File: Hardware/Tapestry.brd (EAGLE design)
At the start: 100 x 80 mm, 81 parts, among them U1 ATSAMS70NXXA-AN, U2 AK4618VQ, U3 V_REG_MIC2920, U4 V_REG_MIC2920, U5 USD-SOCKETNEW, Y1 12MHZ

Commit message: Second update from Jamie
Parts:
- R15: value 330 -> 15K
- R16: value 330 -> 22K
- moved R7 65.6 mm to (8.89, 31.8)
- moved D1 64.8 mm to (8.89, 27.9), turned to 270 degrees
- moved JP2 41.2 mm to (31.8, 8.89), turned to 270 degrees
- moved C13 35.3 mm to (49.5, 47.0), turned to 90 degrees
- moved C14 31.8 mm to (52.1, 47.0), turned to 90 degrees
- moved TP2 31.0 mm to (27.9, 57.1)
- moved C15 28.2 mm to (54.6, 47.0), turned to 90 degrees
- moved U3 27.9 mm to (68.6, 15.2)
- moved U4 26.1 mm to (69.8, 34.3)
- moved C1 25.9 mm to (40.6, 43.2)
- moved C16 24.7 mm to (57.1, 47.0), turned to 90 degrees
- moved C38 22.6 mm to (66.0, 57.1)
- moved C37 22.6 mm to (66.0, 53.3)
- moved TP3 21.8 mm to (6.35, 55.9)
- moved C17 21.1 mm to (59.7, 47.0), turned to 90 degrees
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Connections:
- removed net RD: TP2.6
- removed net TD: TP2.5
- net TDMI: now also TP2.6
- net TDMO: now also TP2.5
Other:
- board size 100 x 80 mm -> 96.2 x 67.3 mm

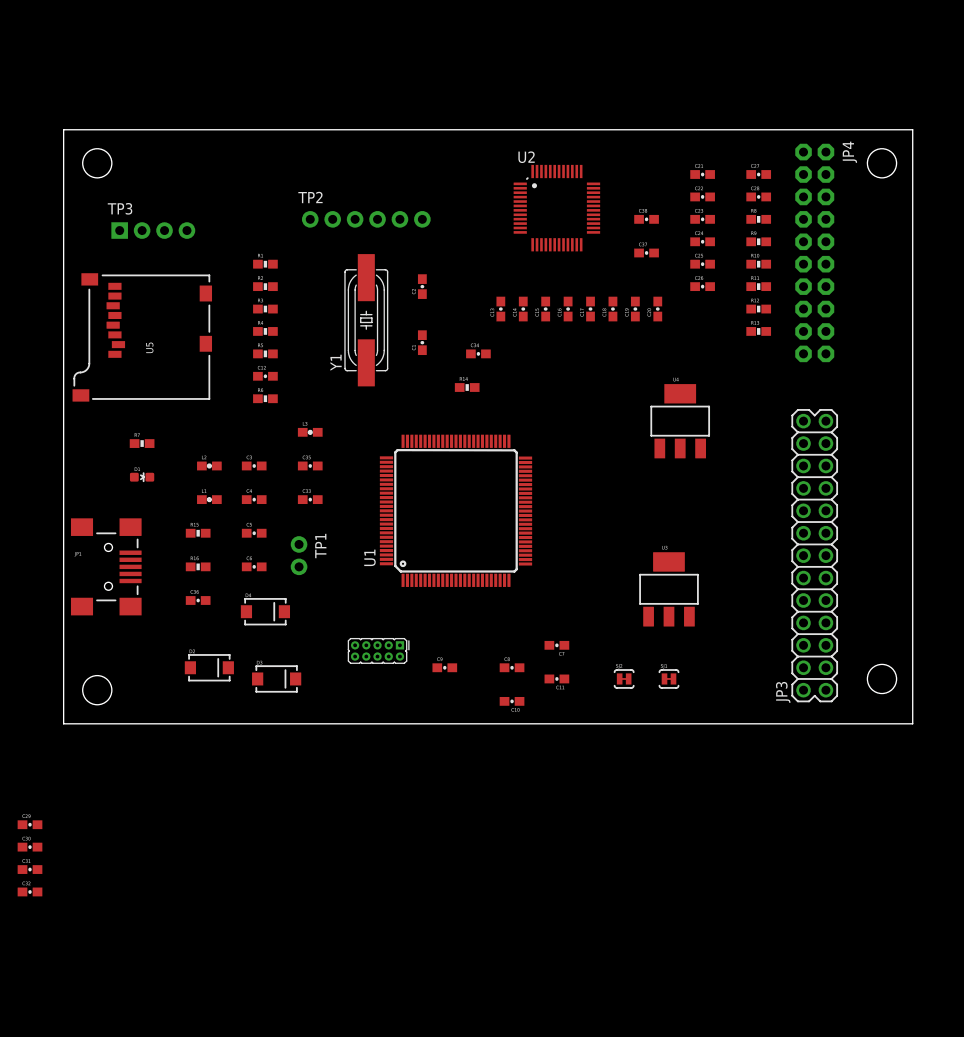
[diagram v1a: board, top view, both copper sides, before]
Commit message: Fixed unconnected nets and missing cap values.
Signed-off-by: robertsonics <jamie@robertsonics.com>
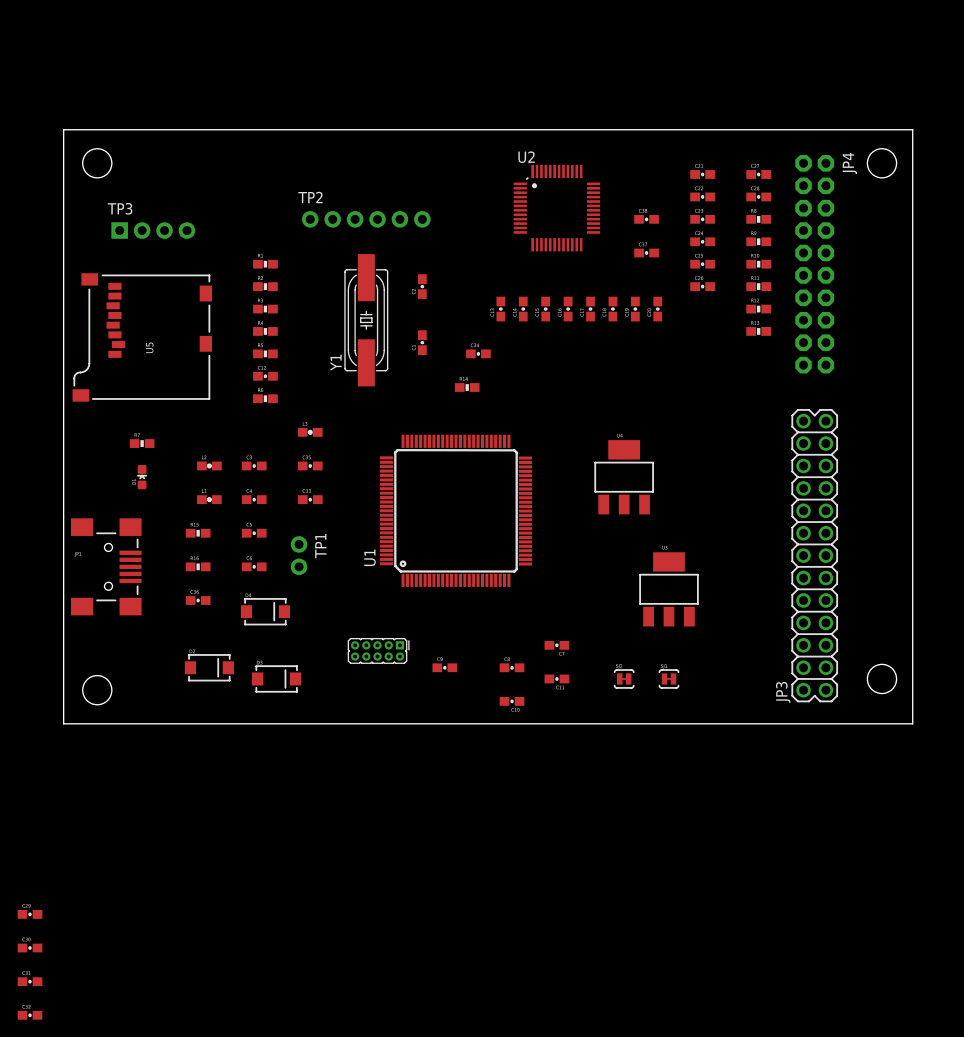
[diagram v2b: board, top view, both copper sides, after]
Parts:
- C29, C30, C31, C32: value (none) -> 0.1uF
- D1: value (none) -> BLUE
- moved C32 14.0 mm to (-3.81, -33.0)
- moved C31 12.7 mm to (-3.81, -29.2)
- moved C30 11.4 mm to (-3.81, -25.4)
- moved C29 10.2 mm to (-3.81, -21.6)
- moved U4 8.98 mm to (63.5, 27.9)
- moved JP4 1.27 mm to (85.1, 52.1)
- turned D1 to 0 degrees
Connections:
- removed net JP1: JP2.1
- removed net N$24: SJ2.2
- removed net TCK: JP2.4
- removed net TMS: JP2.2
- net 3.3V: now also JP2.1
- net 3.3V_A: now also SJ2.2
- net SWCLK/TCK: now also JP2.4
- net SWDIO/TMS: now also JP2.2

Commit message: Replaced generic resistors and capacitors with SparkFun versions.
Signed-off-by: robertsonics <jamie@robertsonics.com>
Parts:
- C13, C15, C17, C19, C20, C21, C22, C23, C24, C25, C26, C27, C28, C37, C38: value 1uF -> 1.0uF
- C34: value 10p -> 10pF
- R1, R8: value 100K -> 100k
- R5: value 10k -> 10K

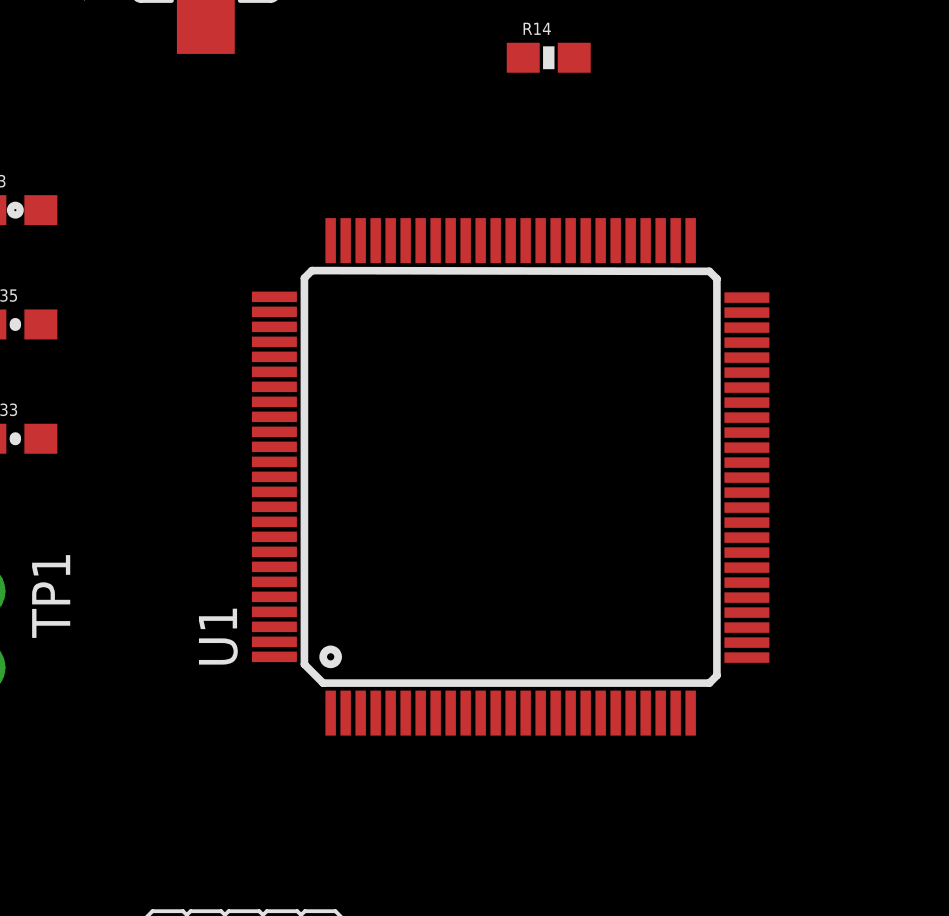
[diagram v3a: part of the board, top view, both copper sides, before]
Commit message: First pass over schematic.
Mostly changing flag style on signals.
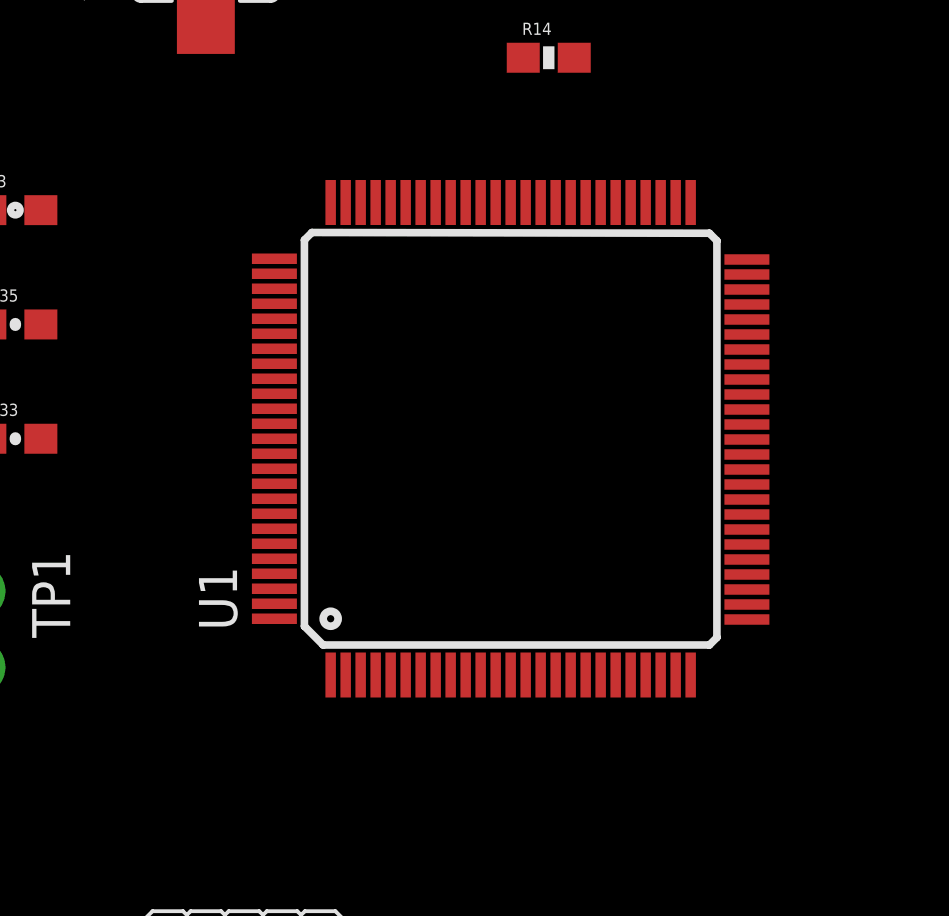
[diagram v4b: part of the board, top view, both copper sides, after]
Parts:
- moved U1 1.27 mm to (44.5, 25.4)

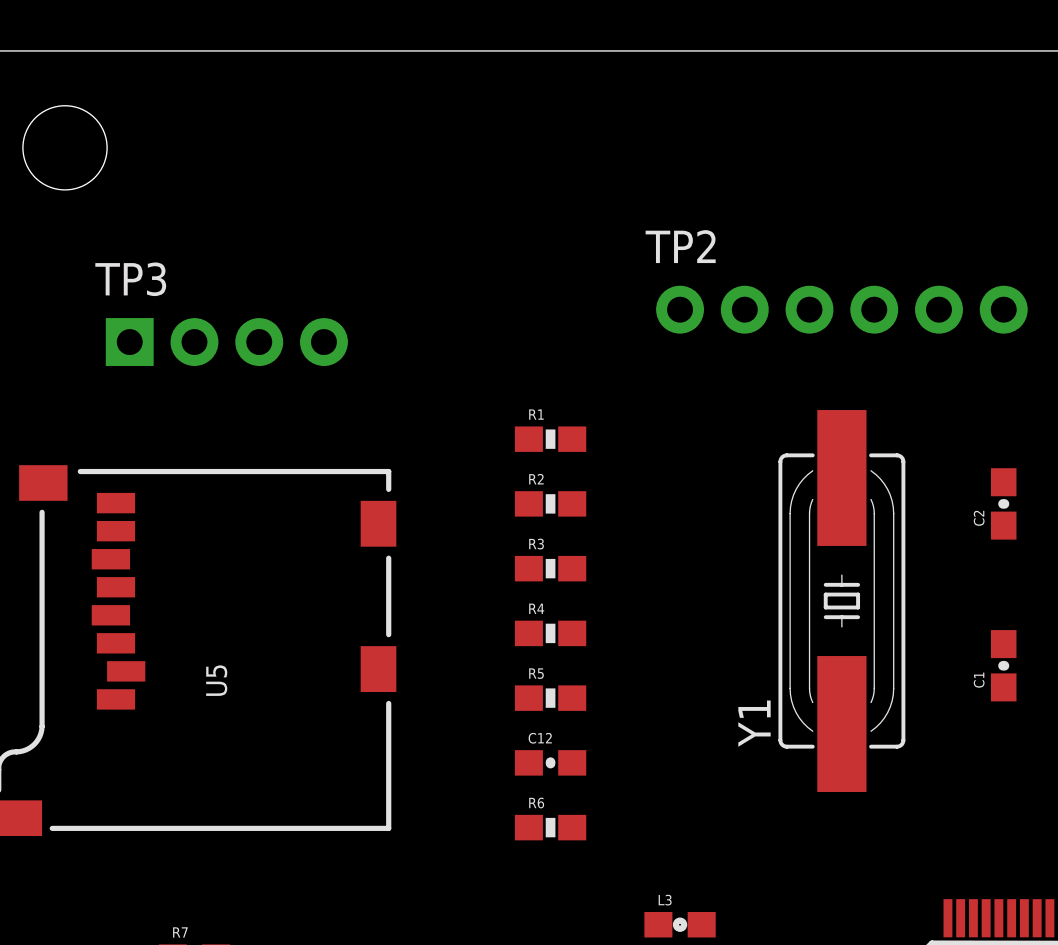
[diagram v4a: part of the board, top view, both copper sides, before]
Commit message: Second pass over schematic
-Swapped crystal for smaller one.
-Updated SD card connector with SDIO signal names.
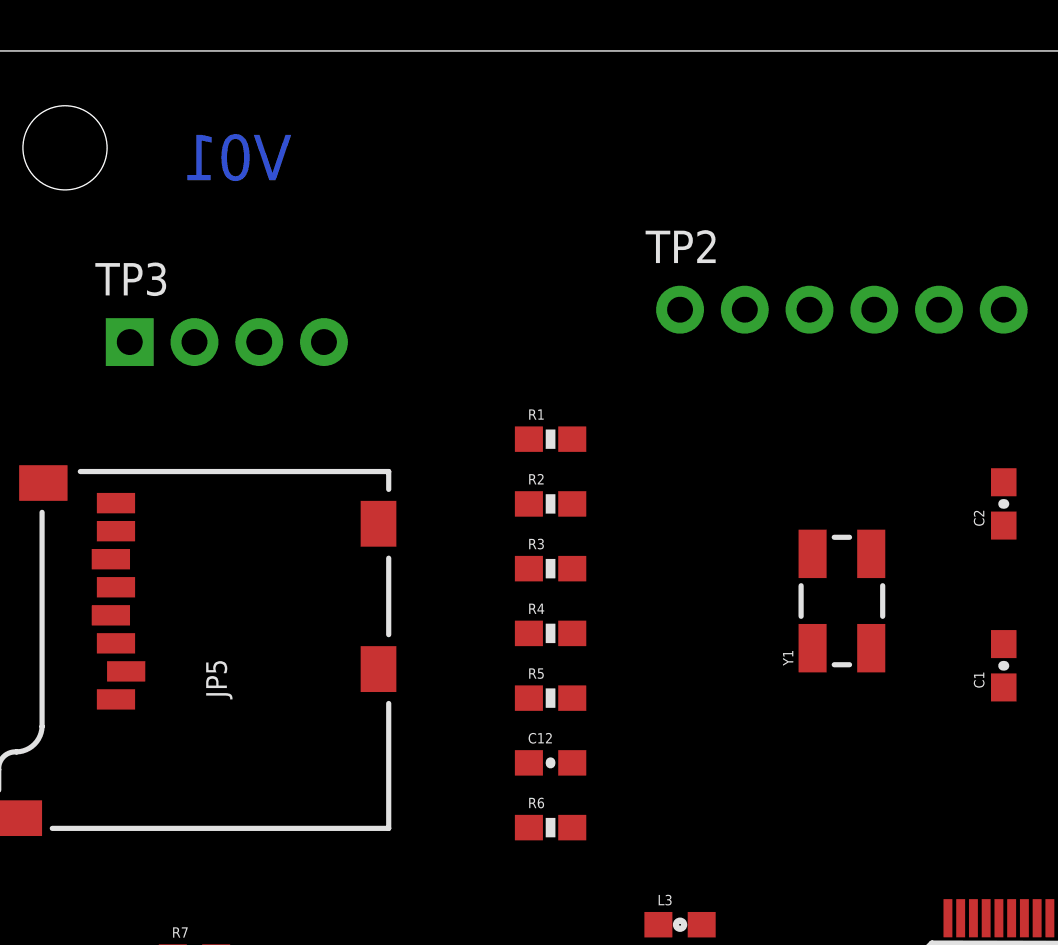
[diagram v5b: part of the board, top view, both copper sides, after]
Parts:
- removed U5: USD-SOCKETNEW, SparkFun-Connectors:MICRO-SD-SOCKET-PP
- added JP5: USD-SDIO-SOCKET, SparkFun-Connectors:MICRO-SD-SOCKET-SDIO
- Y1: value 12MHZ -> 12MHz; device SparkFun-FreqCtrl:HC49UP -> SparkFun-FreqCtrl:CRYSTAL-SMD-5X3
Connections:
- net 3.3V: now also JP5.VCC; no longer U5.VCC
- net GND: now also JP5.GND, JP5.GND1, JP5.GND3; no longer U5.GND, U5.GND1, U5.GND3
- net N$1: now also Y1.3; no longer Y1.2
- net SDCD: now also JP5.CD1, JP5.CD2; no longer U5.CD1, U5.CD2
- net SDCLK: now also JP5.CLK; no longer U5.SCLK
- net SDCMD: now also JP5.CMD; no longer U5.DI
- net SDD0: now also JP5.DAT0; no longer U5.DO
- net SDD1: now also JP5.DAT1; no longer U5.RSV2
- net SDD2: now also JP5.DAT2; no longer U5.RSV1
- net SDD3: now also JP5.CD/DAT3; no longer U5.CS
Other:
- board text added: "Jamie Robertson & Byron Jacquot"
- board text added: "V01"

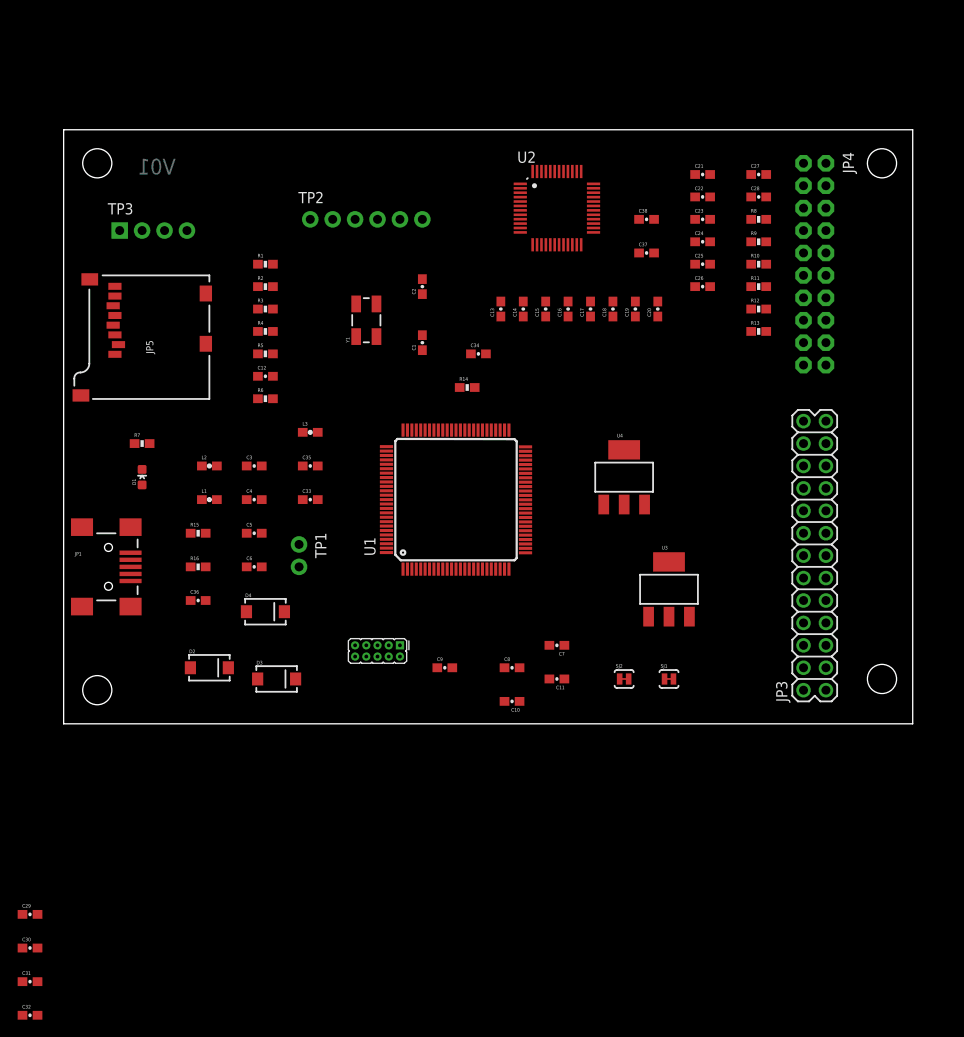
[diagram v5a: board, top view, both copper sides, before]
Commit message: A little more WIP
-uSD socket had SDIO naming on pins.
-pushed parts around PCB.
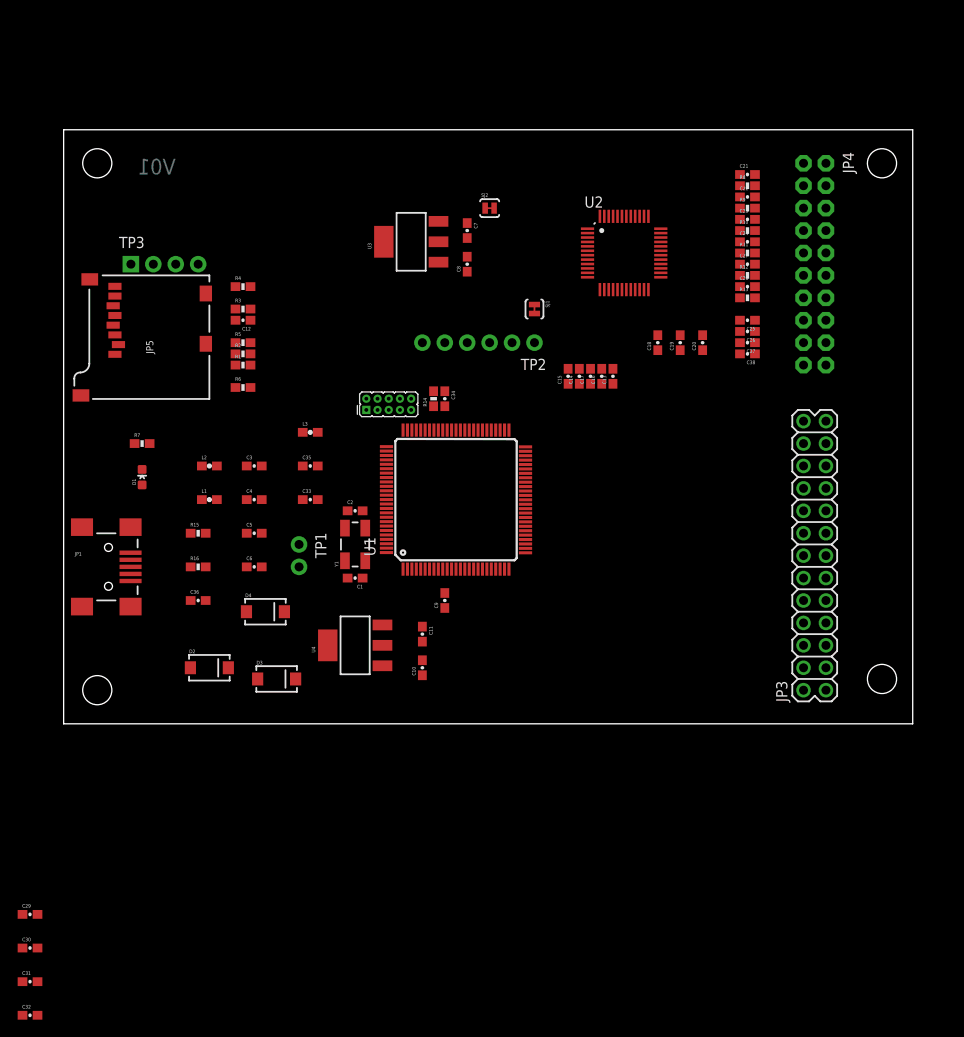
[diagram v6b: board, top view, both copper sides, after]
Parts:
- moved SJ2 55.5 mm to (48.3, 58.4)
- moved U3 49.0 mm to (39.4, 54.6), turned to 90 degrees
- moved C7 48.1 mm to (45.7, 55.9), turned to 270 degrees
- moved C8 46.0 mm to (45.7, 52.1), turned to 90 degrees
- moved SJ1 44.6 mm to (53.3, 47.0), turned to 270 degrees
- moved U4 35.9 mm to (33.0, 8.89), turned to 90 degrees
- moved TP2 29.0 mm to (53.3, 43.2), turned to 180 degrees
- moved C1 27.7 mm to (33.0, 16.5), turned to 180 degrees
- moved JP2 26.8 mm to (34.3, 35.6)
- moved C2 26.5 mm to (33.0, 24.1), turned to 0 degrees
- moved Y1 25.4 mm to (33.0, 20.3)
- moved C38 19.0 mm to (77.5, 41.9), turned to 180 degrees
- moved C11 16.1 mm to (40.6, 10.2), turned to 270 degrees
- moved C37 15.3 mm to (77.5, 43.2), turned to 180 degrees
- moved C13 14.8 mm to (62.2, 39.4)
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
